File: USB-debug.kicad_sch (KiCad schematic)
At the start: 44 parts, among them J4 USB-C_GCT_USB4105-GF-A, Q25 BSS138PW, Q4 BSS138PW, U16 TPD4E05U06QDQARQ1, U31 FT4232H_VQFN, Y2 Oscillator_12MHz_ESC_2520MV

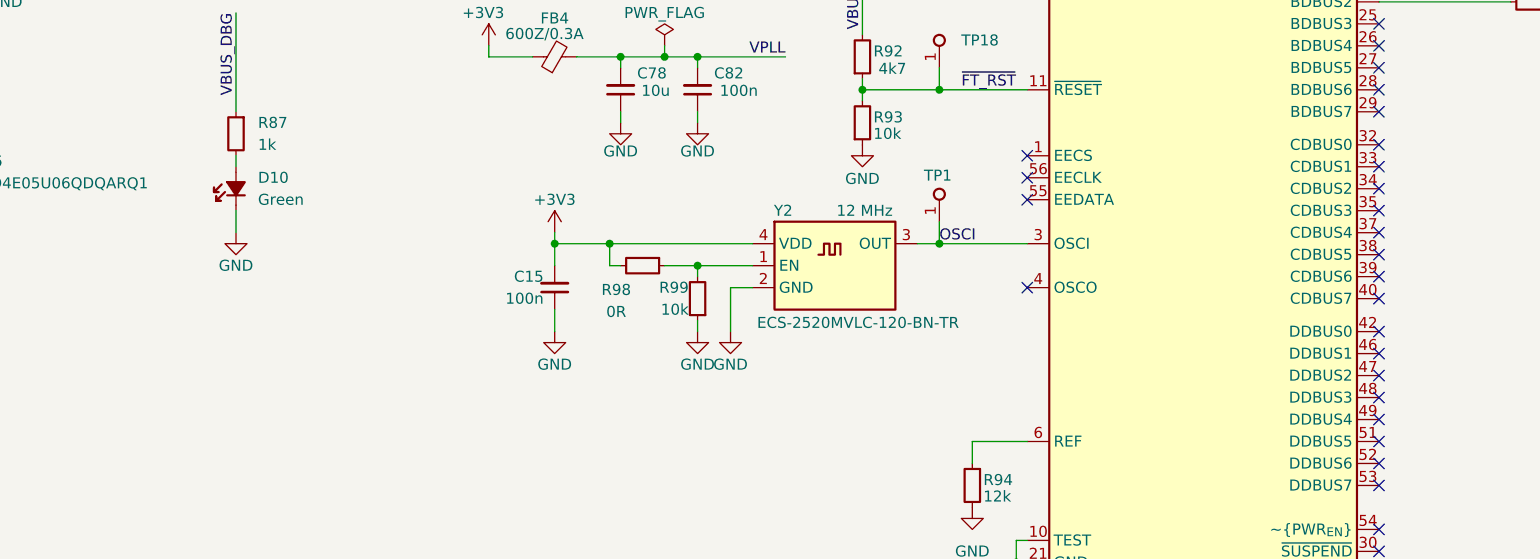
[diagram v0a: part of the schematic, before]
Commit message: made some stupid wrong changes to test the diff tool I'm building.
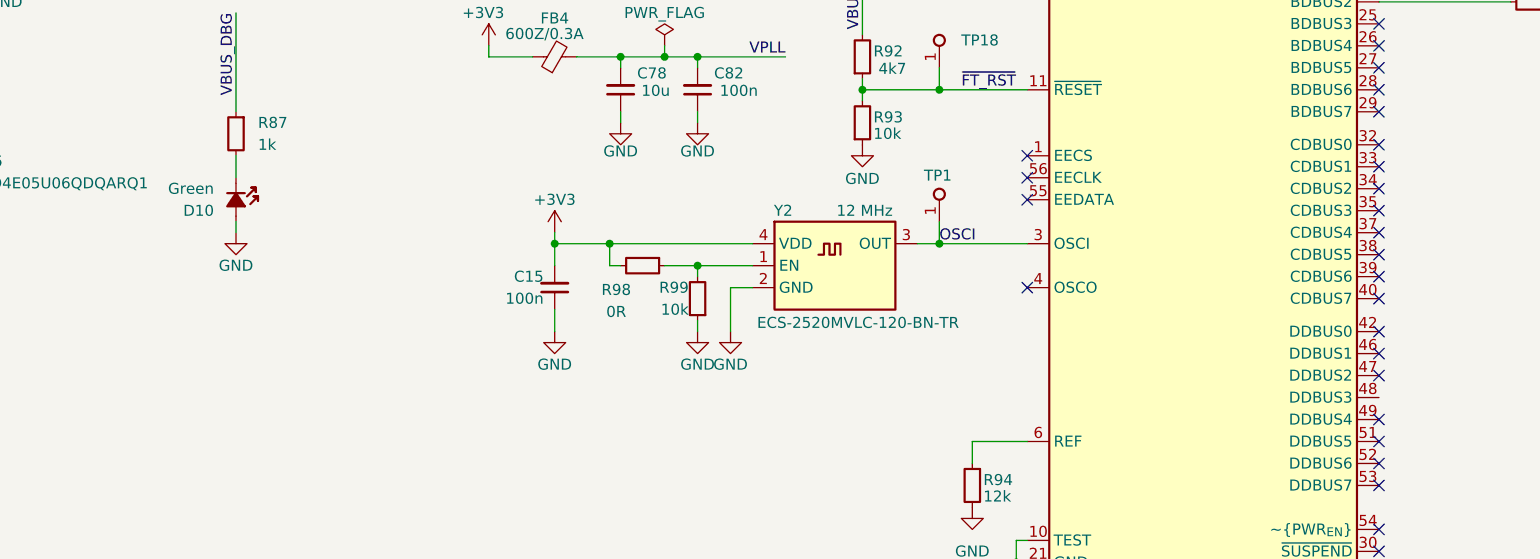
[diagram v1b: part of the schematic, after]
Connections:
- net GND: now also D10.2 (A); no longer D10.1 (C)
- net at R87.2: now also D10.1 (C); no longer D10.2 (A)
- no-connect marks 31 -> 30
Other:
- moved on the sheet: D10
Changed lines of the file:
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@@
 	)
 	(no_connect
-		(at 204.47 130.81)
-	)
-	(no_connect
 		(at 204.47 133.35)
 	)
@@
 	(wire
 		(pts
-			(xy 72.39 109.22) (xy 72.39 111.76)
+			(xy 72.39 105.41) (xy 72.39 102.87)
 		)
 		(stroke
@@
 	(wire
 		(pts
-			(xy 72.39 102.87) (xy 72.39 104.14)
+			(xy 72.39 111.76) (xy 72.39 110.49)
 		)
 		(stroke
@@
 	(symbol
 		(lib_id "antmicroLEDIndicationDiscrete:LED_G_0603_KP-1608CGCK")
-		(at 72.39 109.22 90)
+		(at 72.39 105.41 270)
 		(unit 1)
 		(exclude_from_sim no)
@@
 		(fields_autoplaced yes)
 		(property "Reference" "D10"
-			(at 74.93 105.41 90)
+			(at 69.85 109.22 90)
 			(effects
 				(font
@@
 		)
 		(property "Value" "LED_G_0603_KP-1608CGCK"
-			(at 80.01 86.36 0)
+			(at 64.77 128.27 0)
 			(effects
 				(font
@@
 		)
 		(property "Footprint" "antmicro-footprints:LED_0603_1608Metric_G"
-			(at 82.55 86.36 0)
+			(at 62.23 128.27 0)
 			(effects
 				(font
@@
 		)
 		(property "Datasheet" "http://www.kingbright.com/attachments/file/psearch//000/00/00/KP-1608CGCK(Ver.23B).pdf"
-			(at 85.09 86.36 0)
+			(at 59.69 128.27 0)
 			(effects
 				(font
@@
 		)
 		(property "Description" "LED, Green, SMD, 0603, 20 mA, 2.1 V, 570 nm"
-			(at 72.39 109.22 0)
+			(at 72.39 105.41 0)
 			(effects
 				(font
@@
 		)
 		(property "MPN" "KP-1608CGCK"
-			(at 87.63 86.36 0)
+			(at 57.15 128.27 0)
 			(effects
 				(font
@@
 		)
 		(property "Manufacturer" "Kingbright"
-			(at 90.17 86.36 0)
+			(at 54.61 128.27 0)
 			(effects
 				(font
@@
 		)
 		(property "Color" "Green"
-			(at 74.93 107.9499 90)
+			(at 69.85 106.6801 90)
 			(effects
 				(font
@@
 		)
 		(property "Author" "Antmicro"
-			(at 92.71 86.36 0)
+			(at 52.07 128.27 0)
 			(effects
 				(font
@@
 		)
 		(property "License" "Apache-2.0"
-			(at 95.25 86.36 0)
+			(at 49.53 128.27 0)
 			(effects
 				(font
@@
 		)
 		(instances
-			(project ""
+			(project "led-panel"
 				(path "/a86e1cab-ea0a-45e6-9194-d44b0d5c9450/4155e8b1-3e20-438f-8975-680719ad641f"
 					(reference "D11")
@@
 		)
 		(instances
-			(project ""
+			(project "led-panel"
 				(path "/a86e1cab-ea0a-45e6-9194-d44b0d5c9450/4155e8b1-3e20-438f-8975-680719ad641f"
 					(reference "#FLG01")
